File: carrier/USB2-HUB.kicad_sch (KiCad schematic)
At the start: 32 parts, among them J10 690-008-221-904, J11 Conn_02x05_Odd_Even, J9 USB_OTG, U5 FSUSB42MUX, U6 USB2514B-I/M2, U7 TPD4EUSB30, U8 AP22653W6, Y2 24MHz

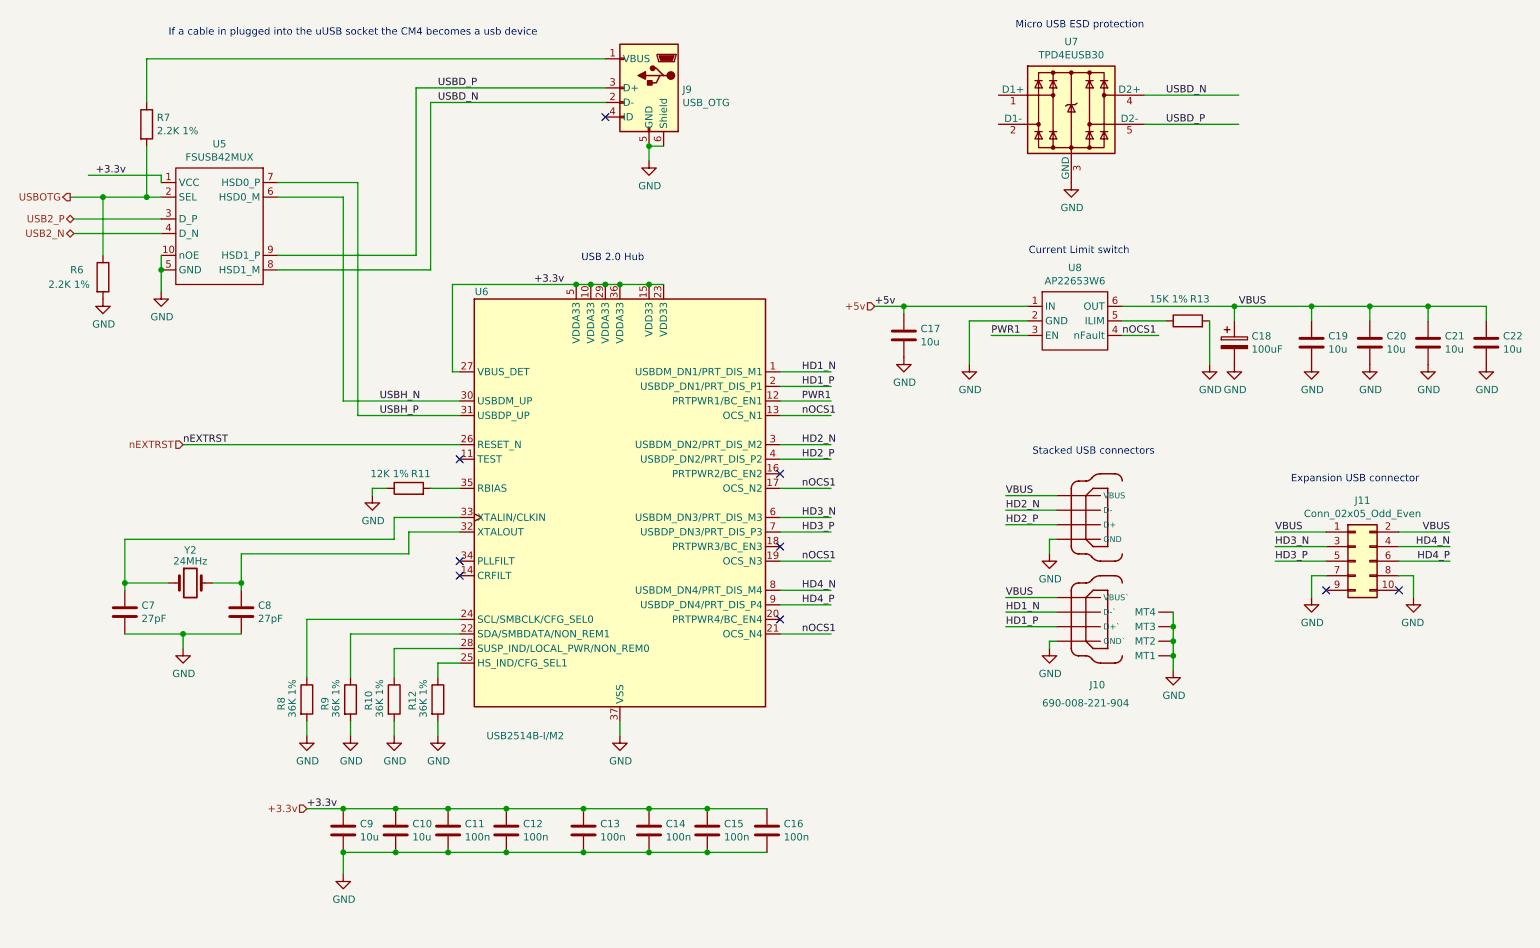
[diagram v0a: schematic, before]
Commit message: Feat: added all sensors, neopixel, buzzer and usb-c to carrier board
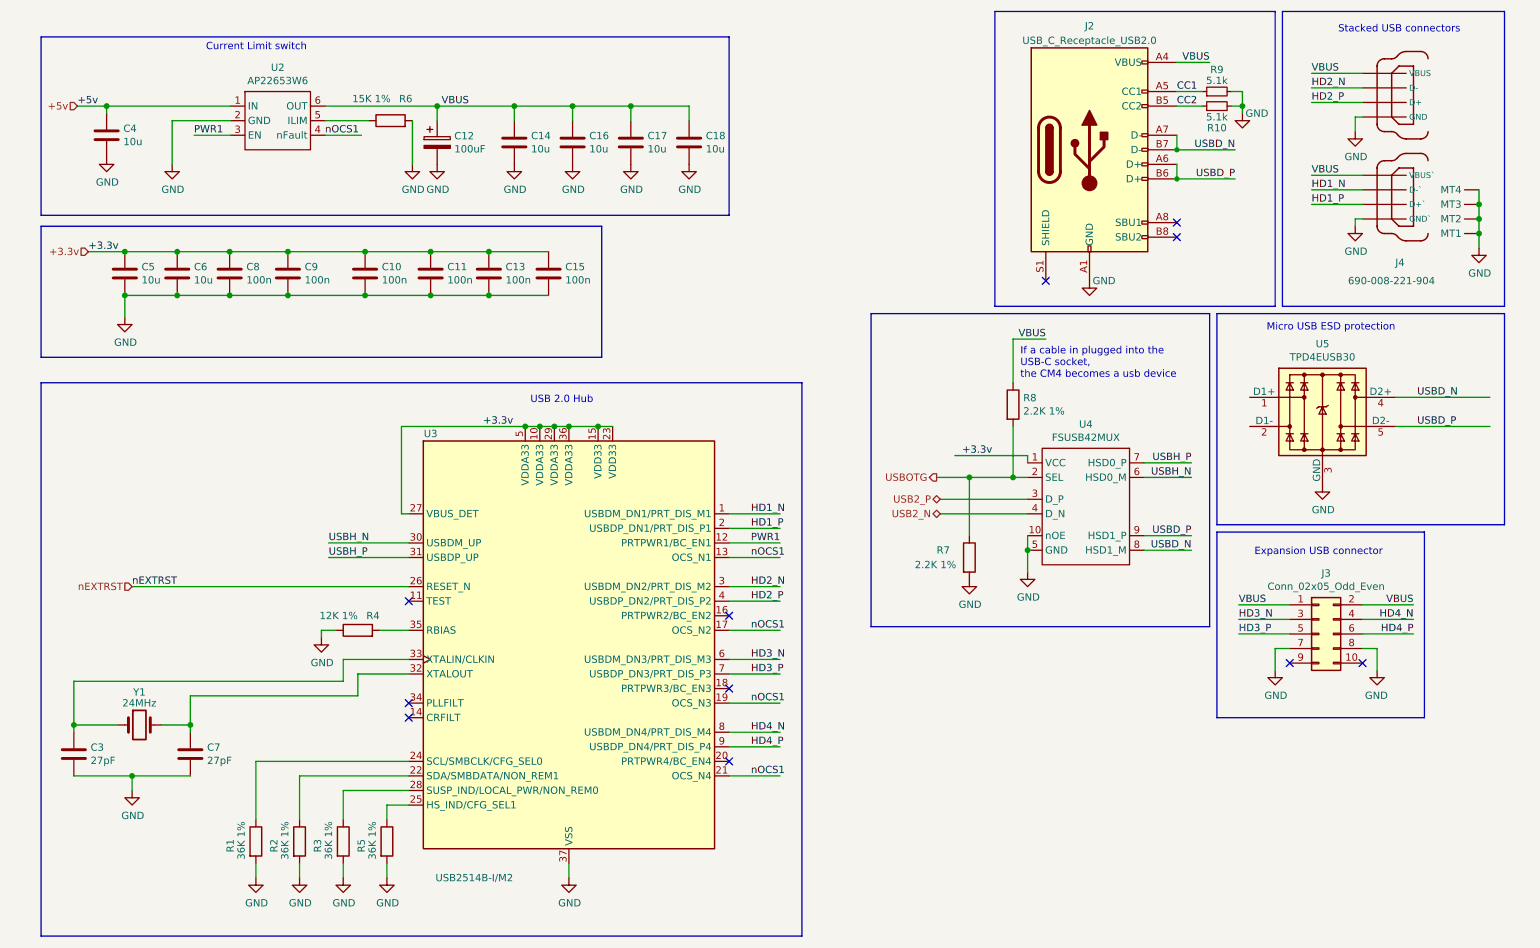
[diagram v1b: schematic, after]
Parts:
- removed J9: USB_OTG, CM4IO:USB_Micro-B_EDAC_UCON00686, symbol Connector:USB_OTG
- added J2: USB_C_Receptacle_USB2.0, symbol Connector:USB_C_Receptacle_USB2.0
- added R10, R9: 5.1k, mikoto:Resistor_0402_1005M-nosilk, symbol Device:R_Small
- renumbered C13 to C10, C14 to C11, C18 to C12, C15 to C13, C19 to C14, C16 to C15, C20 to C16, C21 to C17, C22 to C18, C7 to C3, C17 to C4, C9 to C5, C10 to C6, C8 to C7, C11 to C8, C12 to C9, J11 to J3, J10 to J4, R8 to R1, R9 to R2, R10 to R3, R11 to R4, R12 to R5, R13 to R6, R6 to R7, R7 to R8, U8 to U2, U6 to U3, U5 to U4, U7 to U5, Y2 to Y1
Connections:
- net GND: now also J2.A1 (GND), J2.A12 (GND), J2.B1 (GND), J2.B12 (GND), R10.2, R9.2
- net USBD_N: now also J2.A7 (D-), J2.B7 (D-)
- net USBD_P: now also J2.A6 (D+), J2.B6 (D+)
- net VBUS: now also R8.1, J2.A4 (VBUS), J2.A9 (VBUS), J2.B4 (VBUS), J2.B9 (VBUS)
- new net CC1: J2.A5 (CC1), R9.1
- new net CC2: J2.B5 (CC2), R10.1
- no-connect marks 9 -> 11
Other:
- note added: "If a cable in plugged into the USB-C socket, the CM4 becomes a usb device"
- note removed: "If a cable in plugged into the uUSB socket the CM4 becomes a usb device"
- company: (none) -> MUREX
- title: (none) -> CM4 USB HUB
- moved on the sheet: C10, C11, C12, C13, C14, C15, C16, C17, C18, C3, C4, C5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

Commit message: Feat: carrier board synchronized footprints with schematic
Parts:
- J2: footprint (none) -> Connector_USB:USB_C_Receptacle_HRO_TYPE-C-31-M-12
- R10, R9: footprint mikoto:Resistor_0402_1005M-nosilk -> Resistor_SMD:R_0603_1608Metric
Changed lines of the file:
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@@
       (effects (font (size 1.27 1.27)))
     )
-    (property "Footprint" "mikoto:Resistor_0402_1005M-nosilk" (at 227.965 40.005 0)
+    (property "Footprint" "Resistor_SMD:R_0603_1608Metric" (at 227.965 40.005 0)
       (effects (font (size 1.27 1.27)) hide)
     )
@@
       (effects (font (size 1.27 1.27)))
     )
-    (property "Footprint" "mikoto:Resistor_0402_1005M-nosilk" (at 227.965 37.465 0)
+    (property "Footprint" "Resistor_SMD:R_0603_1608Metric" (at 227.965 37.465 0)
       (effects (font (size 1.27 1.27)) hide)
     )
@@
       (effects (font (size 1.27 1.27)))
     )
-    (property "Footprint" "" (at 209.55 47.625 0)
-      (effects (font (size 1.27 1.27)) hide)
-    )
+    (property "Footprint" "Connector_USB:USB_C_Receptacle_HRO_TYPE-C-31-M-12" (at 209.55 47.625 0)
+      (effects (font (size 1.27 1.27)) hide)
+    )

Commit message: Fix: fixed 3D models for carrier board
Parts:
- renumbered R8 to R10, R9 to R11, R10 to R12, R1 to R3, R2 to R4, R3 to R5, R4 to R6, R5 to R7, R6 to R8, R7 to R9

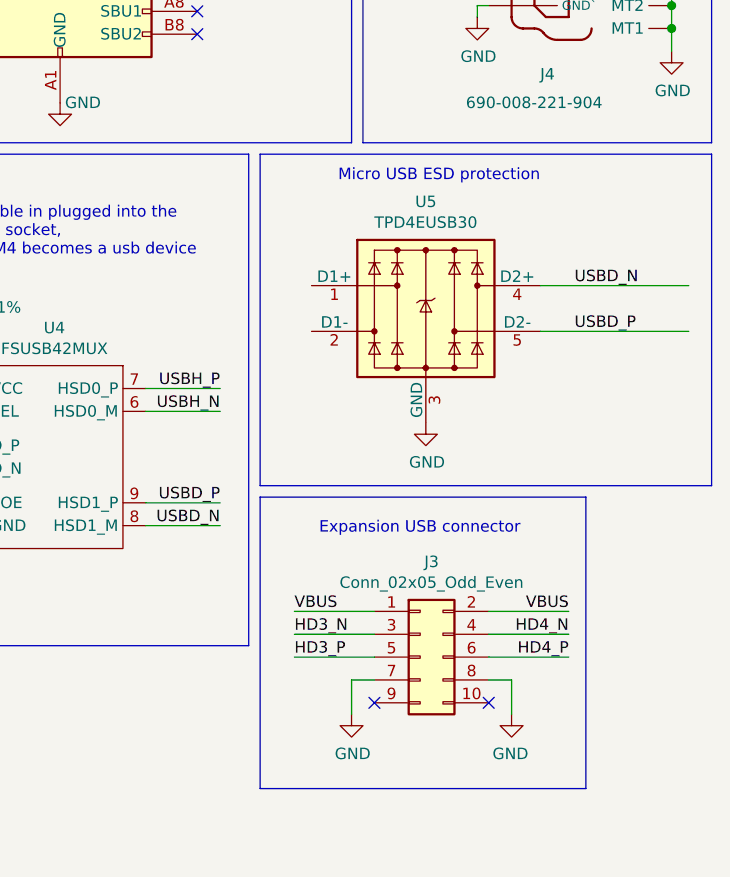
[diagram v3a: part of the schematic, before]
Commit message: Fix: minor labeling and test pad fixes
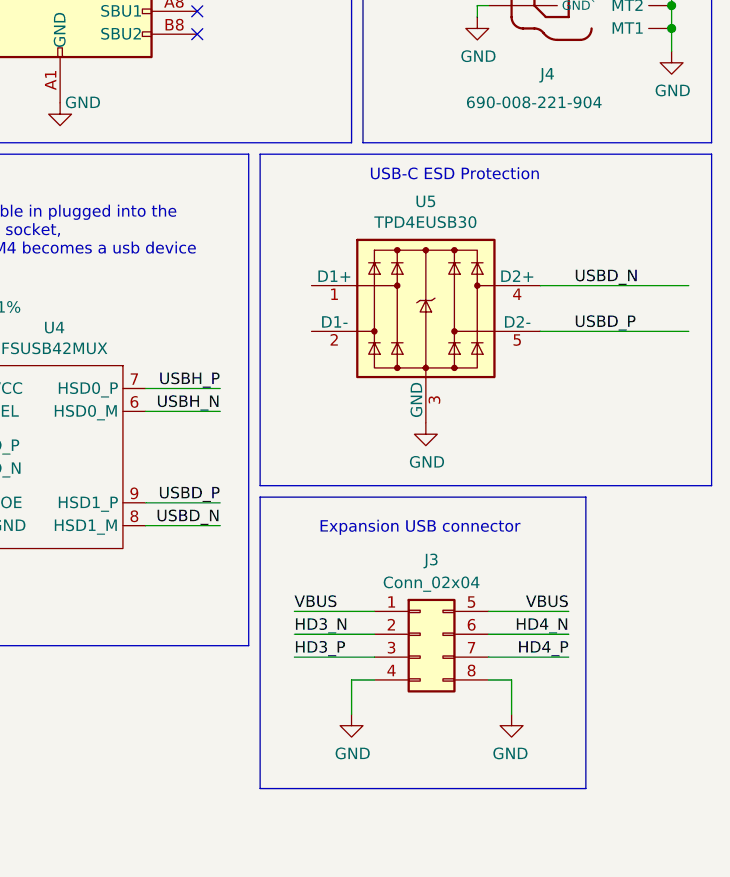
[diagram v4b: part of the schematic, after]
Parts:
- removed J3: Conn_02x05_Odd_Even, Connector_PinHeader_2.54mm:PinHeader_2x05_P2.54mm_Vertical, symbol Connector_Generic:Conn_02x05_Odd_Even
- added J3: Conn_02x04, symbol Connector_Generic:Conn_02x04_Top_Bottom
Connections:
- net GND: now also J3.4 (Pin_4), J3.8 (Pin_8)
- net HD3_N: now also J3.2 (Pin_2)
- net HD3_P: now also J3.3 (Pin_3)
- net HD4_N: now also J3.6 (Pin_6)
- net HD4_P: now also J3.7 (Pin_7)
- net VBUS: now also J3.1 (Pin_1), J3.5 (Pin_5)
- no-connect marks 11 -> 9
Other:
- note added: "USB-C ESD Protection"
- note removed: "Micro USB ESD protection"

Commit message: Fix: relinked footprints
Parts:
- J3: footprint (none) -> Connector_PinHeader_2.54mm:PinHeader_2x04_P2.54mm_Vertical
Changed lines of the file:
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@@
       (effects (font (size 1.27 1.27)))
     )
-    (property "Footprint" "" (at 245.745 129.54 0)
+    (property "Footprint" "Connector_PinHeader_2.54mm:PinHeader_2x04_P2.54mm_Vertical" (at 245.745 129.54 0)
       (effects (font (size 1.27 1.27)) hide)
     )

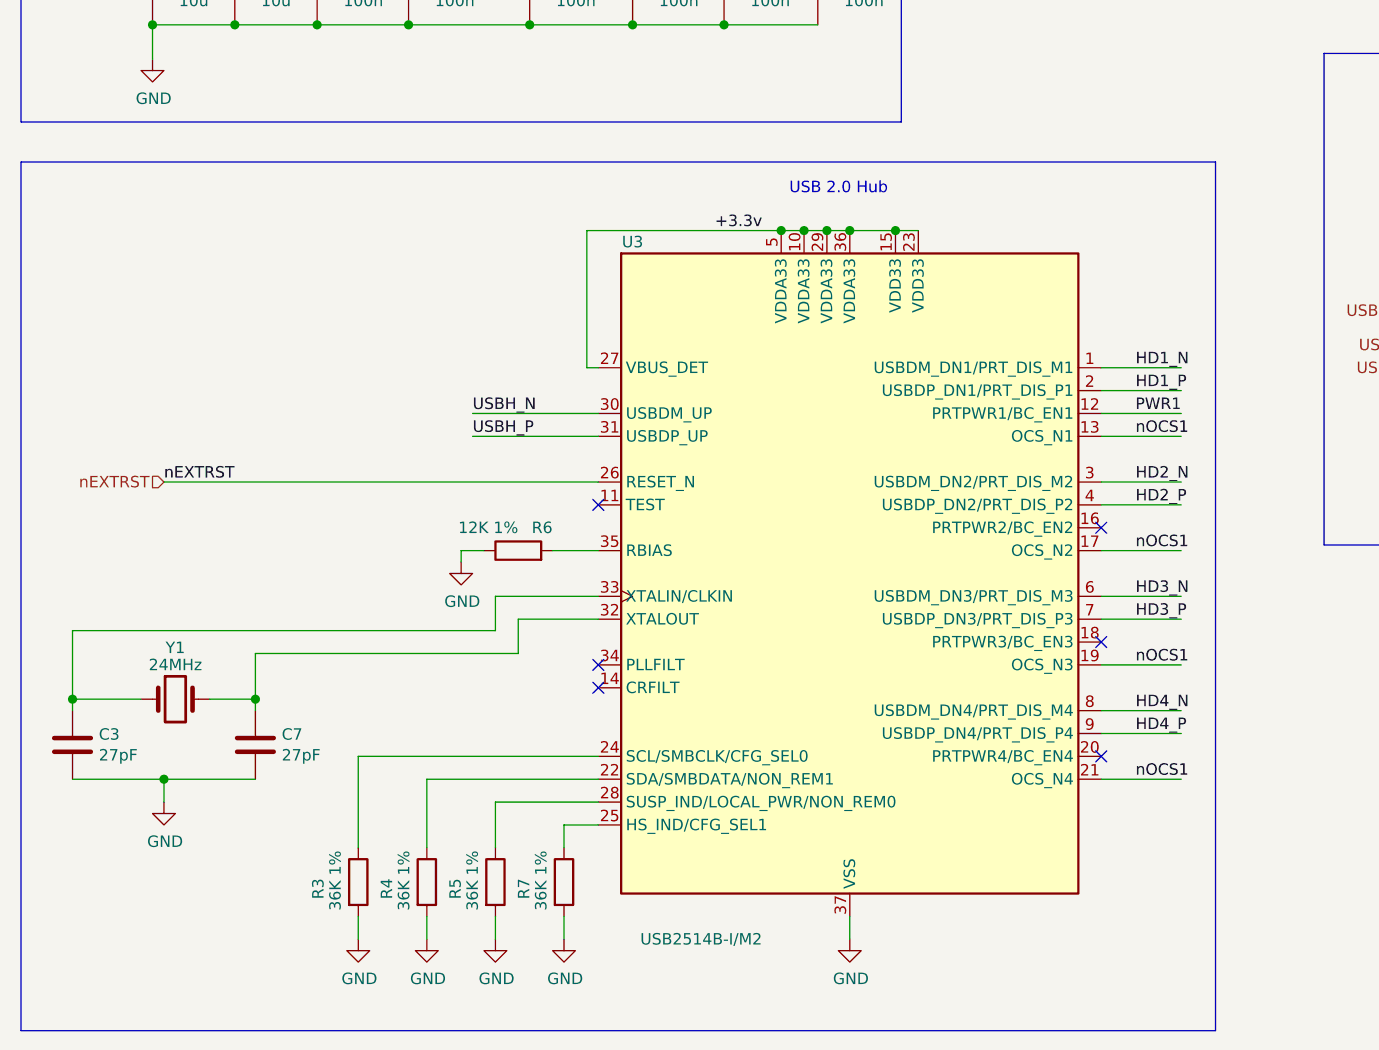
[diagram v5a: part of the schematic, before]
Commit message: Feat: begun work on finalizing PCB layout
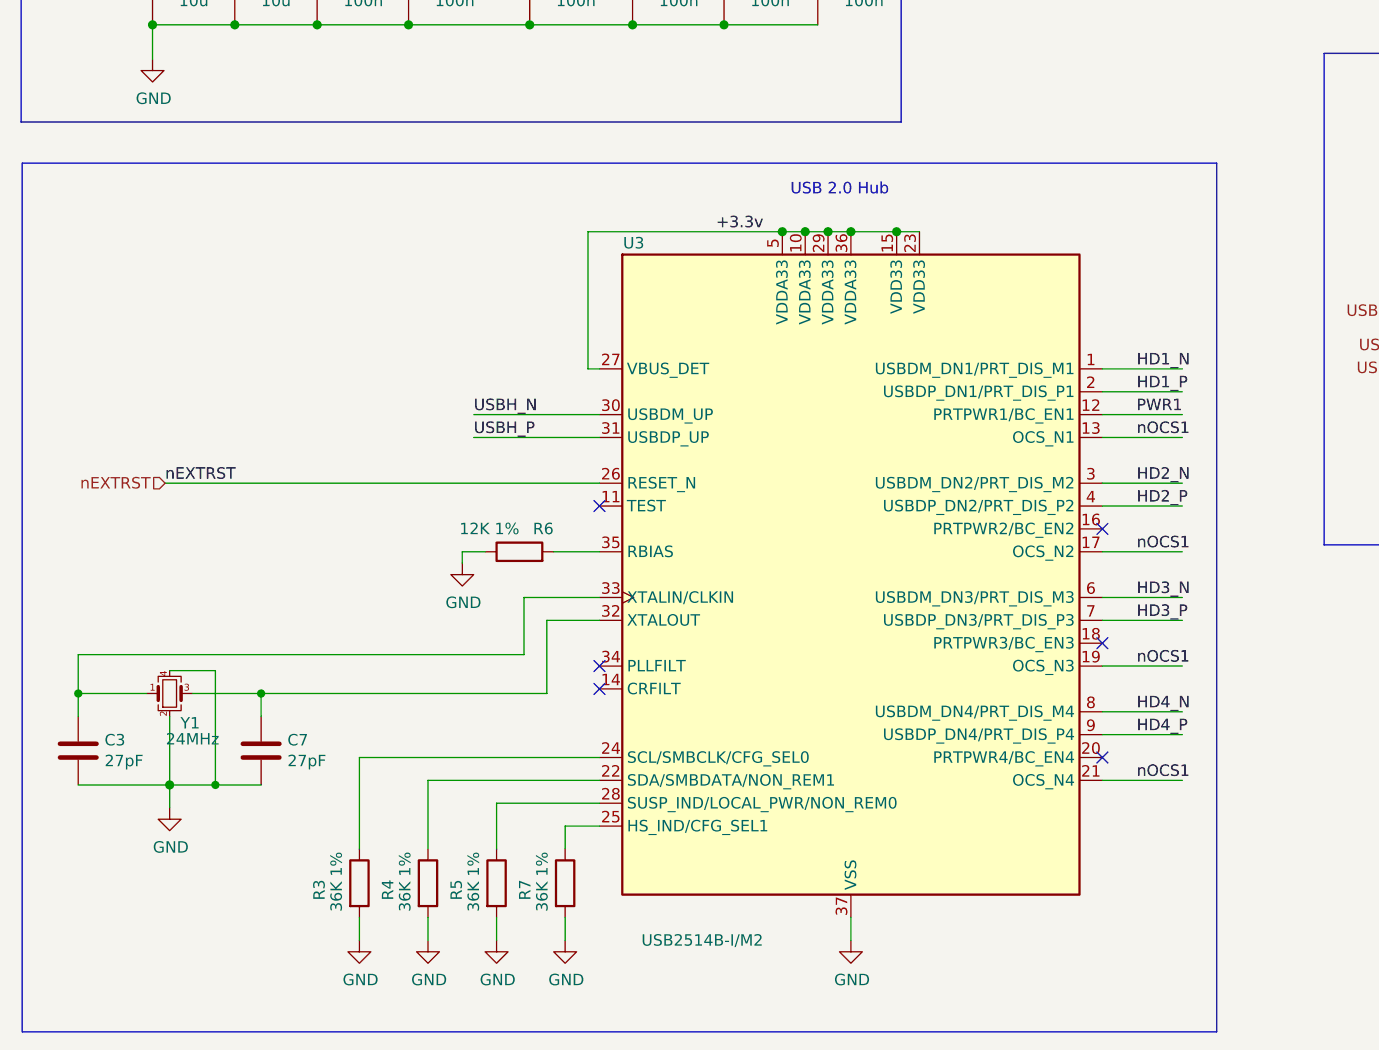
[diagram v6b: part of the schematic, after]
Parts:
- removed Y1: 24MHz, Crystal:Crystal_SMD_HC49-SD, symbol Device:Crystal
- added Y1: 24MHz, Crystal:Crystal_SMD_SeikoEpson_FA238-4Pin_3.2x2.5mm, symbol Device:Crystal_GND24_Small
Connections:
- net GND: now also Y1.2, Y1.4
- net at C7.1, U3.32 (XTALOUT): now also Y1.3
- net at C3.1, U3.33 (XTALIN/CLKIN): now also Y1.1
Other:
- moved on the sheet: C3, C7
